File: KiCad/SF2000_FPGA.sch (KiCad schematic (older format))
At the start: 21 parts, among them J10 Conn_02x01, J11 Conn_02x01, J3 Conn_02x05_Odd_Even, J4 Conn_02x01, J8 Conn_02x01, J9 Conn_02x01, U20 AT25SF081B-SSH, U28 GW1N-UV9LQ144, U8 T8Q144C3

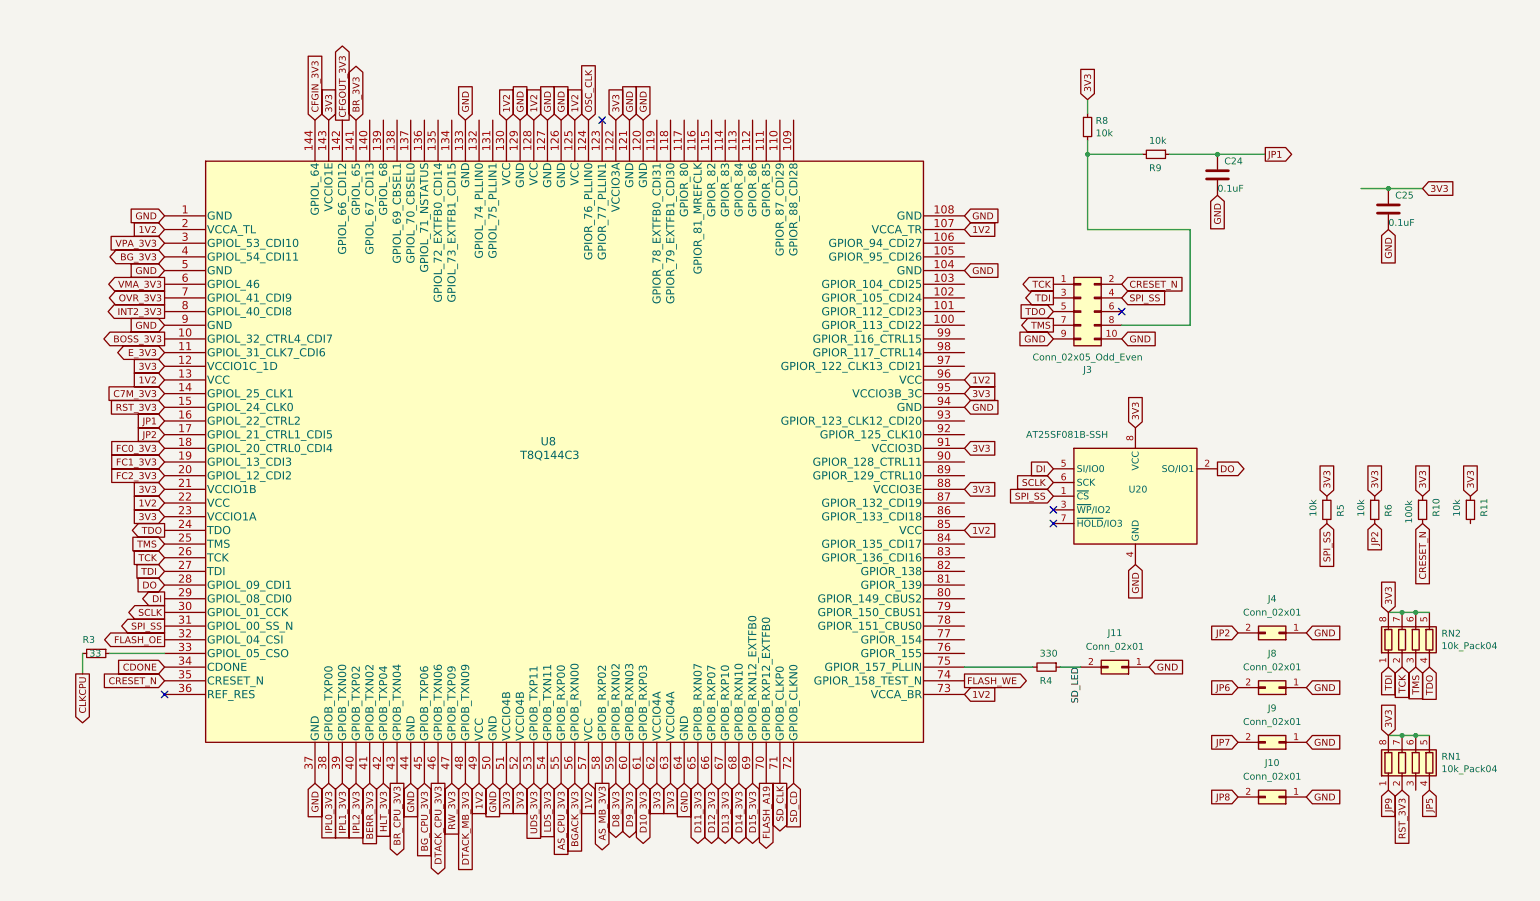
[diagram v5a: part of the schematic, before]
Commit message: Fix placement and routing of components in 4V3 power supply area
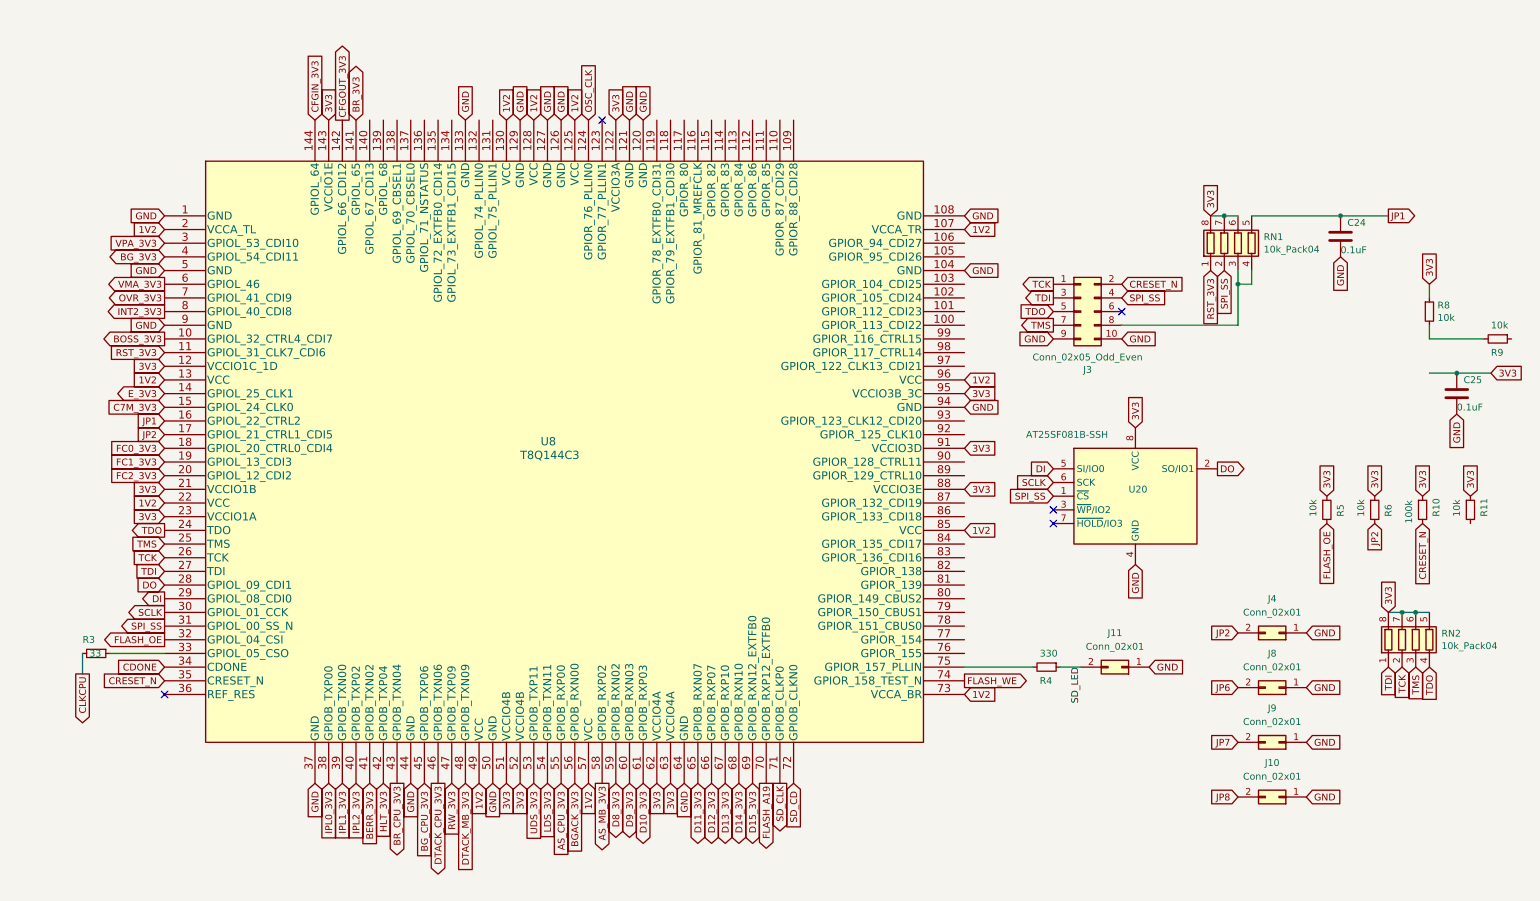
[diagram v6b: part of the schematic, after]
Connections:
- net JP5 is gone; now on an unnamed net: RN1.4 (R4.1)
- net 3V3: no longer RN1.5 (R4.2)
- net C7M_3V3: now also U8.15 (GPIOL_24_CLK0); no longer U8.14 (GPIOL_25_CLK1)
- net E_3V3: now also U8.14 (GPIOL_25_CLK1); no longer U8.11 (GPIOL_31_CLK7_CDI6)
- net FLASH_OE: now also R5.2
- net JP1: now also RN1.5 (R4.2); no longer R9.1
- net JP9: no longer RN1.1 (R1.1)
- net RST_3V3: now also RN1.1 (R1.1), U8.11 (GPIOL_31_CLK7_CDI6); no longer RN1.2 (R2.1), U8.15 (GPIOL_24_CLK0)
- net SPI_SS: now also RN1.2 (R2.1); no longer R5.2
- net at R8.2, R9.2: no longer J3.8 (Pin_8)
- net at RN1.3 (R3.1): now also J3.8 (Pin_8)
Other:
- moved on the sheet: C24, C25, R8, R9, RN1
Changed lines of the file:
@@
 Text GLabel 600  5150 3    50   Output ~ 0
 CLKCPU
-Text GLabel 1200 3100 0    50   Input ~ 0
+Text GLabel 1200 3200 0    50   Input ~ 0
 C7M_3V3
 Text GLabel -2050 6000 3    50   Output ~ 0
@@
 Text GLabel 1200 2000 0    50   Input ~ 0
 VPA_3V3
-Text GLabel 1200 2800 0    50   BiDi ~ 0
+Text GLabel 1200 3100 0    50   BiDi ~ 0
 E_3V3
 Text GLabel 1200 4200 0    50   Input ~ 0
@@
 L Device:R_Pack04 RN1
 U 1 1 625F56E7
-P 10350 5800
-F 0 "RN1" H 10538 5846 50  0000 L CNN
-F 1 "10k_Pack04" H 10538 5755 50  0000 L CNN
-F 2 "SF2000:RESCAF80P320X160X60-8N" V 10625 5800 50  0001 C CNN
-F 3 "~" H 10350 5800 50  0001 C CNN
-	1    10350 5800
-	1    0    0    -1
-$EndComp
-Text GLabel 10150 5600 1    50   Input ~ 0
-3V3
-Text GLabel 10450 6000 3    50   Input ~ 0
-JP5
+P 9050 2000
+F 0 "RN1" H 9238 2046 50  0000 L CNN
+F 1 "10k_Pack04" H 9238 1955 50  0000 L CNN
+F 2 "SF2000:RESCAF80P320X160X60-8N" V 9325 2000 50  0001 C CNN
+F 3 "~" H 9050 2000 50  0001 C CNN
+	1    9050 2000
+	1    0    0    -1
+$EndComp
+Text GLabel 8850 1800 1    50   Input ~ 0
+3V3
 $Comp
 L Device:R_Pack04 RN2
@@
 Wire Wire Line
 	10350 4700 10450 4700
-Text GLabel 7950 950  1    50   Input ~ 0
+Text GLabel 10450 2300 1    50   Input ~ 0
 3V3
 $Comp
@@
 Text GLabel 9550 4850 2    50   Input ~ 0
 GND
-Text GLabel 9250 1350 2    50   Output ~ 0
+Text GLabel 10150 1800 2    50   Output ~ 0
 JP1
 Text GLabel 1200 3400 0    50   Input ~ 0
@@
 Text GLabel 9550 5250 2    50   Input ~ 0
 GND
-Text GLabel 8900 1650 3    50   Input ~ 0
-GND
-Text GLabel 10400 1600 2    50   Input ~ 0
-3V3
-Wire Wire Line
-	8900 1350 9250 1350
+Text GLabel 9800 2100 3    50   Input ~ 0
+GND
+Text GLabel 10900 2950 2    50   Input ~ 0
+3V3
+Wire Wire Line
+	9800 1800 10150 1800
 $Comp
 L Device:C C?
 U 1 1 624A6DA8
-P 8900 1500
+P 9800 1950
 AR Path="/624A6DA8" Ref="C?"  Part="1"
 AR Path="/620D263D/624A6DA8" Ref="C24"  Part="1"
-F 0 "C24" H 8950 1600 50  0000 L CNN
-F 1 "0.1uF" H 8900 1400 50  0000 L CNN
-F 2 "Capacitor_SMD:C_0805_2012Metric_Pad1.15x1.40mm_HandSolder" H 8938 1350 50  0001 C CNN
-F 3 "~" H 8900 1500 50  0001 C CNN
-	1    8900 1500
+F 0 "C24" H 9850 2050 50  0000 L CNN
+F 1 "0.1uF" H 9800 1850 50  0000 L CNN
+F 2 "Capacitor_SMD:C_0805_2012Metric_Pad1.15x1.40mm_HandSolder" H 9838 1800 50  0001 C CNN
+F 3 "~" H 9800 1950 50  0001 C CNN
+	1    9800 1950
 	1    0    0    -1
 $EndComp
@@
 L Device:C C?
 U 1 1 624B4CFC
-P 10150 1750
+P 10650 3100
 AR Path="/624B4CFC" Ref="C?"  Part="1"
 AR Path="/620D263D/624B4CFC" Ref="C25"  Part="1"
-F 0 "C25" H 10200 1850 50  0000 L CNN
-F 1 "0.1uF" H 10150 1650 50  0000 L CNN
-F 2 "Capacitor_SMD:C_0805_2012Metric_Pad1.15x1.40mm_HandSolder" H 10188 1600 50  0001 C CNN
-F 3 "~" H 10150 1750 50  0001 C CNN
-	1    10150 1750
-	1    0    0    -1
-$EndComp
-Text GLabel 10150 1900 3    50   Input ~ 0
-GND
-Wire Wire Line
-	9950 1600 10150 1600
-Connection ~ 10150 1600
-Wire Wire Line
-	10150 1600 10400 1600
+F 0 "C25" H 10700 3200 50  0000 L CNN
+F 1 "0.1uF" H 10650 3000 50  0000 L CNN
+F 2 "Capacitor_SMD:C_0805_2012Metric_Pad1.15x1.40mm_HandSolder" H 10688 2950 50  0001 C CNN
+F 3 "~" H 10650 3100 50  0001 C CNN
+	1    10650 3100
+	1    0    0    -1
+$EndComp
+Text GLabel 10650 3250 3    50   Input ~ 0
+GND
+Wire Wire Line
+	10450 2950 10650 2950
+Connection ~ 10650 2950
+Wire Wire Line
+	10650 2950 10900 2950
 $Comp
 L Device:R_Small R?
 U 1 1 62517BB4
-P 7950 1150
+P 10450 2500
 AR Path="/62517BB4" Ref="R?"  Part="1"
 AR Path="/620D263D/62517BB4" Ref="R8"  Part="1"
-F 0 "R8" H 8009 1196 50  0000 L CNN
-F 1 "10k" H 8009 1105 50  0000 L CNN
-F 2 "Resistor_SMD:R_0805_2012Metric_Pad1.15x1.40mm_HandSolder" H 7950 1150 50  0001 C CNN
-F 3 "~" H 7950 1150 50  0001 C CNN
-	1    7950 1150
+F 0 "R8" H 10509 2546 50  0000 L CNN
+F 1 "10k" H 10509 2455 50  0000 L CNN
+F 2 "Resistor_SMD:R_0805_2012Metric_Pad1.15x1.40mm_HandSolder" H 10450 2500 50  0001 C CNN
+F 3 "~" H 10450 2500 50  0001 C CNN
+	1    10450 2500
 	1    0    0    -1
 $EndComp
@@
 L Device:R_Small R?
 U 1 1 62519236
-P 8450 1350
+P 10950 2700
 AR Path="/62519236" Ref="R?"  Part="1"
 AR Path="/620D263D/62519236" Ref="R9"  Part="1"
-F 0 "R9" V 8550 1300 50  0000 L CNN
-F 1 "10k" V 8350 1300 50  0000 L CNN
-F 2 "Resistor_SMD:R_0805_2012Metric_Pad1.15x1.40mm_HandSolder" H 8450 1350 50  0001 C CNN
-F 3 "~" H 8450 1350 50  0001 C CNN
-	1    8450 1350
+F 0 "R9" V 11050 2650 50  0000 L CNN
+F 1 "10k" V 10850 2650 50  0000 L CNN
+F 2 "Resistor_SMD:R_0805_2012Metric_Pad1.15x1.40mm_HandSolder" H 10950 2700 50  0001 C CNN
+F 3 "~" H 10950 2700 50  0001 C CNN
+	1    10950 2700
 	0    1    1    0
 $EndComp
 Wire Wire Line
-	7950 1050 7950 950
-Wire Wire Line
-	7950 1250 7950 1350
-Wire Wire Line
-	8350 1350 7950 1350
-Wire Wire Line
-	8550 1350 8900 1350
-Connection ~ 8900 1350
+	10450 2400 10450 2300
+Wire Wire Line
+	10450 2600 10450 2700
+Wire Wire Line
+	10850 2700 10450 2700
+Connection ~ 9800 1800
 $Comp
 L Device:R_Small R?
@@
 Text Label 7900 5100 3    50   ~ 0
 SD_LED
-Text GLabel 10150 6000 3    50   Input ~ 0
-JP9
 Text GLabel -5700 3550 0    50   Input ~ 0
 JP9
-Wire Wire Line
-	7950 1900 7950 1350
-Connection ~ 7950 1350
 Text GLabel 1200 2100 0    50   BiDi ~ 0
 BG_3V3
@@
 	0    1    1    0
 $EndComp
-Text GLabel 1200 3200 0    50   Input ~ 0
+Text GLabel 1200 2800 0    50   Input ~ 0
 RST_3V3
 Connection ~ -4550 1100
@@
 	1    0    0    -1
 $EndComp
-Text GLabel 10250 6000 3    50   Input ~ 0
+Text GLabel 8850 2200 3    50   Input ~ 0
 RST_3V3
 Text GLabel -1900 1100 1    50   Input ~ 0
@@
 Text GLabel 8200 2300 2    50   Input ~ 0
 CRESET_N
-Wire Wire Line
-	8700 1900 8700 2600
-Wire Wire Line
-	7950 1900 8700 1900
-Wire Wire Line
-	8200 2600 8700 2600
-Wire Wire Line
-	10450 5600 10350 5600
-Connection ~ 10250 5600
-Wire Wire Line
-	10250 5600 10150 5600
-Connection ~ 10350 5600
-Wire Wire Line
-	10350 5600 10250 5600
+Connection ~ 8950 1800
+Wire Wire Line
+	8950 1800 8850 1800
+Wire Wire Line
+	9050 1800 8950 1800
 NoConn ~ 1200 5300
 Text GLabel 10050 4050 3    50   Input ~ 0
@@
 Wire Wire Line
 	600  5000 600  5150
-Text GLabel 9700 4050 3    50   Input ~ 0
+Text GLabel 8950 2200 3    50   Input ~ 0
 SPI_SS
 Text GLabel 8200 2400 2    50   Input ~ 0
@@
 Wire Wire Line
 	7050 5100 7550 5100
+Wire Wire Line
+	9050 2200 9050 2300
+Wire Wire Line
+	9050 2300 9150 2300
+Wire Wire Line
+	9150 2300 9150 2200
+Connection ~ 9050 2300
+Wire Wire Line
+	9050 2300 9050 2600
+Wire Wire Line
+	9150 1800 9800 1800
+Wire Wire Line
+	8200 2600 9050 2600
+Text GLabel 9700 4050 3    50   Input ~ 0
+FLASH_OE
 $EndSCHEMATC

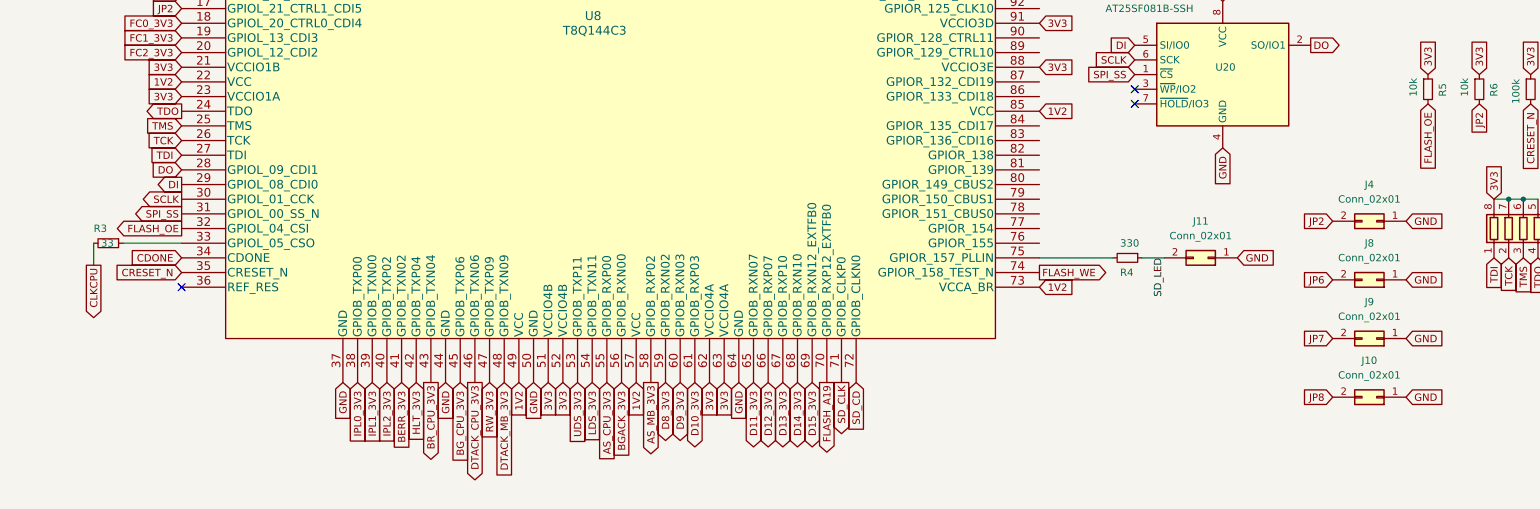
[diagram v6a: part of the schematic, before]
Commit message: Remove IDE-header, add Clockport-header, fixed routing of AVEC and FLASH_OE signals and pull-ups
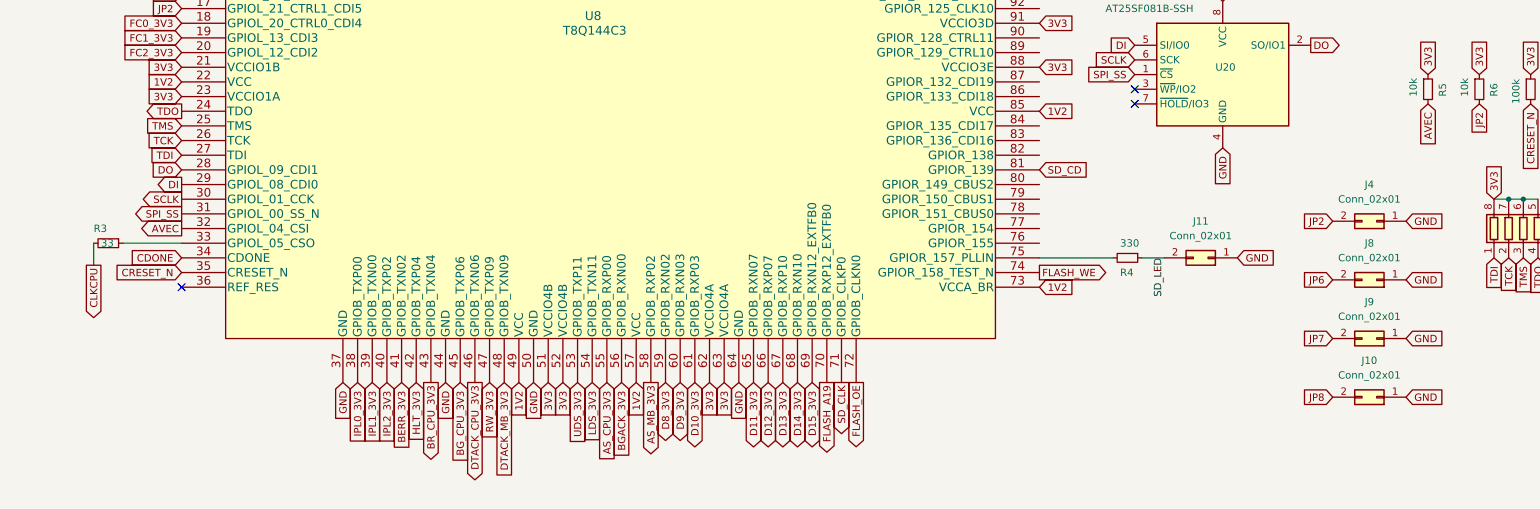
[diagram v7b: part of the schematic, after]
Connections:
- net FLASH_OE: now also U8.72 (GPIOB_CLKN0); no longer R5.2, U8.32 (GPIOL_04_CSI)
- net SD_CD: now also U8.81 (GPIOR_139); no longer U8.72 (GPIOB_CLKN0)
- new net AVEC: R5.2, U8.32 (GPIOL_04_CSI)
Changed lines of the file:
@@
 Text GLabel 5700 5950 3    50   Output ~ 0
 SD_CLK
-Text GLabel 5800 5950 3    50   Input ~ 0
+Text GLabel 7050 4500 2    50   Input ~ 0
 SD_CD
 Text GLabel -800 3100 2    50   BiDi ~ 0
@@
 Text GLabel -800 5300 2    50   Input ~ 0
 JP8
-Text GLabel 1200 4900 0    50   Output ~ 0
+Text GLabel 5800 5950 3    50   Output ~ 0
 FLASH_OE
 Text GLabel -2150 6000 3    50   Output ~ 0
@@
 Wire Wire Line
 	8200 2600 9050 2600
+Text GLabel 1200 4900 0    50   Output ~ 0
+AVEC
 Text GLabel 9700 4050 3    50   Input ~ 0
-FLASH_OE
+AVEC
 $EndSCHEMATC
